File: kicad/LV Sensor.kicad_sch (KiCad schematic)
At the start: 22 parts, among them U1 MCP2518FD-xJHA, U2 LMR51603Y3DBVR, U3 XMSM0C1104SPW20R, U4 AP63205WU-7, U5 ATA6561-GAQW-N, U6 DSC1001DL5, U7 ADS114S06BIPBSR, U8 LM2662MX/NOPB

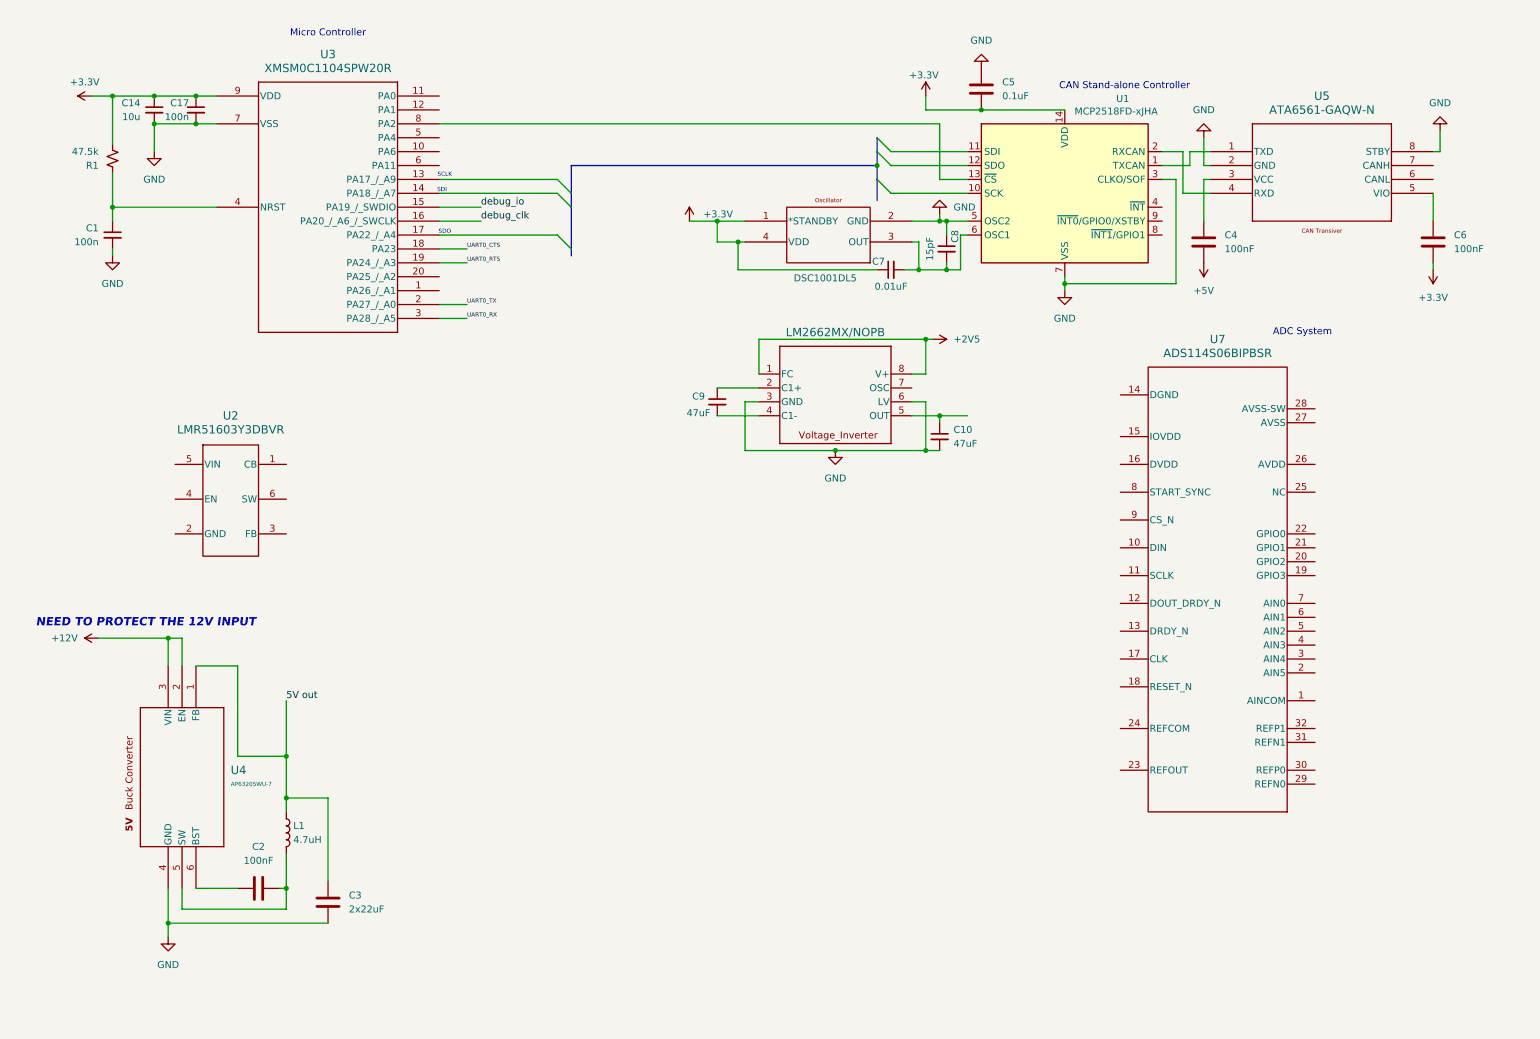
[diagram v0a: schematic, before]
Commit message: Pretty much finished everything for now. Just need to condition the analog inputs.
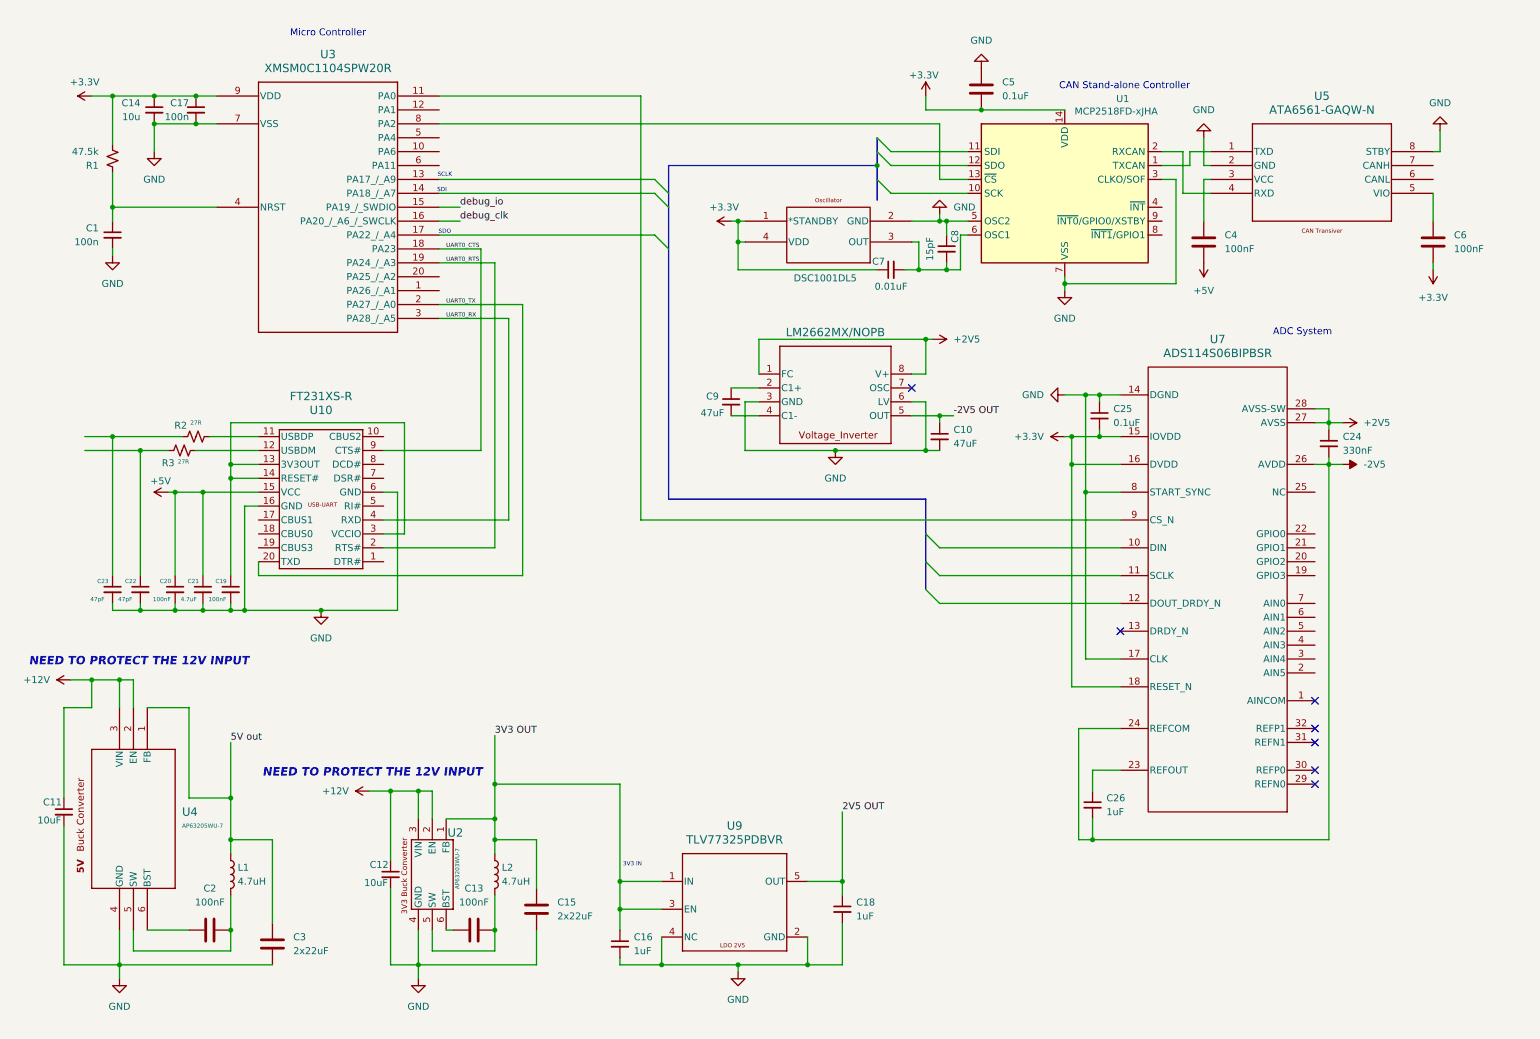
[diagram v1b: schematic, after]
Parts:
- removed U2: LMR51603Y3DBVR, DBV0006A-MFG-IPC_A, symbol LV-Sensor-Lib:LMR51603Y3DBVR
- added C11, C12: 10uF, symbol Device:C_Small
- added C13: 100nF, symbol Device:C
- added C15: 2x22uF, symbol Device:C
- added C16, C18, C26: 1uF, symbol Device:C_Small
- added C19, C20: 100nF, symbol Device:C_Small
- added C21: 4.7uF, symbol Device:C_Small
- added C22, C23: 47pF, symbol Device:C_Small
- added C24: 330nF, symbol Device:C_Small
- added C25: 0.1uF, symbol Device:C_Small
- added L2: 4.7uH, symbol Device:L
- added R2, R3: 27R, symbol Device:R_Small_US
- added U10: FT231XS-R, SSOP-20_FTD, symbol LV-Sensor-Lib:FT231XS-R
- added U2: AP63203WU-7, AP63203WU-7_DIO, symbol LV-Sensor-Lib:AP63203WU-7
- added U9: TLV77325PDBVR, DBV0005A-IPC_A, symbol LV-Sensor-Lib:TLV77325PDBVR
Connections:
- net +12V: now also C11.1, C12.1, U2.2 (EN), U2.3 (VIN)
- net +2V5: now also U7.27 (AVSS), U7.28 (AVSS-SW), C24.1
- net +3.3V: now also U7.15 (IOVDD), U7.16 (DVDD), U7.18 (RESET_N), C25.2
- net +5V: now also C20.1, C21.1, U10.15 (VCC)
- net GND: now also U7.14 (DGND), U7.17 (CLK), U7.8 (START_SYNC), C11.2, C12.2, C15.1, C16.2, C18.2, C19.2, C20.2, C21.2, C22.2, C23.2, C25.1, U10.16 (GND), U10.6 (GND), U2.4 (GND), U9.2 (GND), U9.4 (NC)
- net UART0_CTS: now also U10.9 (CTS#)
- net UART0_RTS: now also U10.2 (RTS#)
- net UART0_RX: now also U10.4 (RXD)
- net UART0_TX: now also U10.20 (TXD)
- net -2V5 OUT: now reaches C10.1, U8.5 (OUT)
- net at U7.23 (REFOUT): now also C26.1
- net -2V5: now reaches U7.24 (REFCOM)
- net -2V5: now also U7.26 (AVDD), C24.2, C26.2
- net at U7.9 (CS_N): now also U3.11 (PA0)
- new net: C23.1, R2.1
- new net: C22.1, R3.1
- new net: R3.2, U10.12 (USBDM)
- new net: R2.2, U10.11 (USBDP)
- new net: C19.1, U10.13 (3V3OUT), U10.14 (RESET#), U10.3 (VCCIO)
- new net: C13.1, U2.6 (BST)
- new net: C13.2, L2.2, U2.5 (SW)
- new net 2V5 OUT: C18.1, U9.5 (OUT)
- new net 3V3 OUT: C15.2, C16.1, L2.1, U2.1 (FB), U9.1 (IN), U9.3 (EN)
- no-connect marks 0 -> 7
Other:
- note added: "3V3 IN"
- moved on the sheet: C2, C3, C9, L1, U4

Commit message: 09-05-2025 Finished Revision.1 of LV Sensor Board
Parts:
- added C27: 22uF, Capacitor_SMD:C_1206_3216Metric_Pad1.33x1.80mm_HandSolder, symbol Device:C
- C1, C17: specs 100nF, 250VDC, X7R, 10%, -55C, +125C -> 100nF, 250VDC, X7R, +/-10%, -55C to +125C; unit x10 0.062 -> 0.042
- C10, C9: footprint (none) -> Capacitor_SMD:C_1206_3216Metric_Pad1.33x1.80mm_HandSolder; mouser (none) -> https://www.mouser.com/ProductDetail/Walsin/1206N470J500CT?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; specs (none) -> 47 pF, 60VDC, +/-5%, -55C to 125C; unit x10 (none) -> 0.058
- C11, C12: footprint (none) -> Capacitor_SMD:C_1206_3216Metric_Pad1.33x1.80mm_HandSolder; mouser (none) -> https://www.mouser.com/ProductDetail/Walsin/1206X106J250CT?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; specs (none) -> 10 uF, 25 VDC, +/-5%, -55C to +85; unit x10 (none) -> 0.202
- C13, C2: footprint (none) -> Capacitor_SMD:C_1206_3216Metric_Pad1.33x1.80mm_HandSolder; mouser (none) -> https://www.mouser.com/ProductDetail/Murata-Electronics/GRT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; specs (none) -> 0.1 uF, 1% tolerance, -55 to +125C; unit x10 (none) -> 0.583
- C14: unit x10 0.07 -> 00.07
- C15, C3: value 2x22uF -> 22uF; footprint (none) -> Capacitor_SMD:C_1206_3216Metric_Pad1.33x1.80mm_HandSolder; mouser (none) -> https://www.mouser.com/ProductDetail/Samsung-Electro-Mechan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; specs (none) -> 22 uF, 25VDC, +/-10%, -55C to +85C; unit x10 (none) -> 0.076
- C16, C18, C26: footprint (none) -> Capacitor_SMD:C_1206_3216Metric_Pad1.33x1.80mm_HandSolder; mouser (none) -> https://www.mouser.com/ProductDetail/Samsung-Electro-Mechan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; specs (none) -> 1uF, 50 VDC, +/-10%, -55C to +125C; unit x10 (none) -> 0.049
- C19, C20, C4, C6: footprint (none) -> Capacitor_SMD:C_1206_3216Metric_Pad1.33x1.80mm_HandSolder; mouser (none) -> https://www.mouser.com/ProductDetail/Walsin/0402B104K100CT?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; specs (none) -> 0.1 uF, 10VDC, +/-10%, -55C to +125C; unit x10 (none) -> 00.04
- C21: footprint (none) -> Capacitor_SMD:C_1206_3216Metric_Pad1.33x1.80mm_HandSolder; mouser (none) -> https://www.mouser.com/ProductDetail/Samsung-Electro-Mechan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; specs (none) -> 4.7 uF, 25 VDC,+/-10%, -55C to +125C; unit x10 (none) -> 0.067
- C22, C23: footprint (none) -> Capacitor_SMD:C_1206_3216Metric_Pad1.33x1.80mm_HandSolder; mouser (none) -> https://www.mouser.com/ProductDetail/Walsin/1206B474K100CT?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; specs (none) -> 0.47 uF, 10 VDC, +/-10%, -55C to +125; unit x10 (none) -> 0.076
- C24: footprint (none) -> Capacitor_SMD:C_1206_3216Metric_Pad1.33x1.80mm_HandSolder; mouser (none) -> https://www.mouser.com/ProductDetail/Murata-Electronics/GRM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; specs (none) -> 0.33 uF, 63VDC, +/-10%, -55C to +125C; unit x10 (none) -> 0.031
- C25, C5: footprint (none) -> Capacitor_SMD:C_1206_3216Metric_Pad1.33x1.80mm_HandSolder; mouser (none) -> https://www.mouser.com/ProductDetail/Walsin/1206B104K251CT?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; specs (none) -> 100nF, 250VDC, X7R, +/-10%, -55C to +125C; unit x10 (none) -> 0.042
- C7: footprint (none) -> Capacitor_SMD:C_1206_3216Metric_Pad1.33x1.80mm_HandSolder; mouser (none) -> https://www.mouser.com/ProductDetail/Walsin/1206N103F250CT?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; specs (none) -> 0.01uF, 25 VDC, +/-1%, -55C to 125C; unit x10 (none) -> 0.242
- C8: footprint (none) -> Capacitor_SMD:C_1206_3216Metric_Pad1.33x1.80mm_HandSolder; mouser (none) -> https://www.mouser.com/ProductDetail/Walsin/1206N150F500CT?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; specs (none) -> 15 pF, 50 VDC, +/-1%, -55C to +125C; unit x10 (none) -> 00.23
- L1, L2: footprint (none) -> Inductor_SMD:L_TDK_NLV25_2.5x2.0mm; mouser (none) -> https://www.mouser.com/ProductDetail/Wurth-Elektronik/74479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; specs (none) -> 4.7 uH, 128 mOhms, 25 MHz, -55 to +150 C; unit x10 (none) -> 0.311
- R1: unit x10 0.04 -> 00.04
- R2, R3: footprint (none) -> Resistor_SMD:R_1206_3216Metric_Pad1.30x1.75mm_HandSolder; mouser (none) -> https://www.mouser.com/ProductDetail/KOA-Speer/RK73B2BTTD39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; specs (none) -> 39Ohms, 200V,1/4 W, 5%, -55 to +155 C; unit x10 (none) -> 0.022
- U1: footprint LV Sensor:MCP2518FDT -> LV-Sensor-Footprints-Lib:MCP2518FDT; unit x10 19.6 -> 19.60
- U10: footprint SSOP-20_FTD -> LV-Sensor-Footprints-Lib:SSOP-20_FTD; mouser (none) -> https://www.mouser.com/ProductDetail/FTDI/FT231XS-R?qs=Gp1Y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; specs (none) -> 480 Mb/s, USB 2.0, 2.97V-5.5V, 125uA-8mA, -40C to + 85C; unit x10 (none) -> 23.40
- U2: footprint AP63203WU-7_DIO -> LV-Sensor-Footprints-Lib:AP6320xWU-7_DIO; mouser (none) -> https://www.mouser.com/ProductDetail/Diodes-Incorporated/AP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; specs (none) -> 3.8V-3.2V In, 3.3V Out, 2A Out, 3.8V-32V, 1.1MHz, -40C to +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; unit x10 (none) -> 05.06
- U3: footprint TSSOP20_PW_TEX -> LV-Sensor-Footprints-Lib:TSSOP20_PW_TEX; mouser (none) -> https://www.mouser.com/ProductDetail/Texas-Instruments/XMSM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; specs (none) -> 20PIN, 12-bit, 16KB flash, 24MHz CPU, 1.62V-3.6V, 32kHz LFO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; unit x10 (none) -> 05.06
- U4: footprint SOIC_05WU-7_DIO -> LV-Sensor-Footprints-Lib:AP6320xWU-7_DIO; mouser (none) -> https://www.mouser.com/ProductDetail/Diodes-Incorporated/AP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; specs (none) -> 3.8V-3.2V In, 5V Out, 2A Out, 3.8V-32V, 1.1MHz, -40C to +85C; unit x10 (none) -> 05.06
- U5: footprint SOIC8_4P9X3P9MC_MCH -> LV-Sensor-Footprints-Lib:SOIC8_4P9X3P9MC_MCH; mouser (none) -> https://www.mouser.com/ProductDetail/Microchip-Technology/A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; specs (none) -> 5Mb/s, 1 Driver /1 Receiver, 4.5V - 5.5V,50mA Operating Cur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; unit x10 (none) -> 04.80
- U6: footprint CDFN4_2P5X2_MCH -> LV-Sensor-Footprints-Lib:CDFN4_2P5X2_MCH; unit x10 (none) -> 14.00
- U7: footprint PBS0032A_N -> LV-Sensor-Footprints-Lib:PBS0032A_N; unit x10 6.08 -> 60.80
- U8: footprint M08A -> LV-Sensor-Footprints-Lib:M08A; mouser (none) -> https://www.mouser.com/ProductDetail/Texas-Instruments/LM26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; specs (none) -> 200mA, 1.3 mA Operating Current, -1.5 V to -5.5 V, 75kHz, 7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; unit x10 (none) -> 14.10
- U9: footprint DBV0005A-IPC_A -> LV-Sensor-Footprints-Lib:DBV0005A-IPC_A; mouser (none) -> https://www.mouser.com/ProductDetail/Texas-Instruments/TLV7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; specs (none) -> 300-mA, 2.5V Out, 1 Output, 1.4V-5.5V, 600mV Dropout, 80dB 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; unit x10 (none) -> 0.068
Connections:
- net +3.3V: now also C6.1, U5.5 (VIO); no longer C6.2
- net +5V: now also C4.1, U5.3 (VCC); no longer C4.2
- net 5V out: now also C27.2
- net GND: now also C4.2, C6.2, C27.1
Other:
- moved on the sheet: C6

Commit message: 09-05-2025 "Finished" LV-Sensor-Can Board
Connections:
- net +3.3V: no longer U6.1 (*STANDBY)
- no-connect marks 7 -> 8
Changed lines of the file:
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@@
 	)
 	(junction
-		(at 143.51 50.8)
-		(diameter 0)
-		(color 0 0 0 0)
-	)
-	(junction
 		(at 180.34 86.36)
 		(diameter 0)
@@
 	)
 	(no_connect
+		(at 144.78 50.8)
+	)
+	(no_connect
 		(at 248.92 153.67)
 	)
@@
 	(wire
 		(pts
-			(xy 143.51 50.8) (xy 143.51 54.61)
-		)
-		(stroke
-			(width 0)
-			(type default)
-		)
-	)
-	(wire
-		(pts
 			(xy 143.51 54.61) (xy 143.51 59.69)
 		)
@@
 	(wire
 		(pts
-			(xy 142.24 50.8) (xy 143.51 50.8)
+			(xy 138.43 54.61) (xy 143.51 54.61)
 		)
 		(stroke
@@
 	(wire
 		(pts
-			(xy 143.51 50.8) (xy 144.78 50.8)
-		)
-		(stroke
-			(width 0)
-			(type default)
-		)
-	)
-	(wire
-		(pts
 			(xy 208.28 163.83) (xy 251.46 163.83)
 		)
@@
 	(symbol
 		(lib_id "power:+3.3V")
-		(at 142.24 50.8 90)
+		(at 138.43 54.61 90)
 		(unit 1)
 		(exclude_from_sim no)
@@
 		(fields_autoplaced yes)
 		(property "Reference" "#PWR010"
-			(at 146.05 50.8 0)
+			(at 142.24 54.61 0)
 			(effects
 				(font
@@
 		)
 		(property "Value" "+3.3V"
-			(at 140.97 48.26 90)
+			(at 137.16 52.07 90)
 			(effects
 				(font
@@
 		)
 		(property "Footprint" ""
-			(at 142.24 50.8 0)
+			(at 138.43 54.61 0)
 			(effects
 				(font
@@
 		)
 		(property "Datasheet" ""
-			(at 142.24 50.8 0)
+			(at 138.43 54.61 0)
 			(effects
 				(font
@@
 		)
 		(property "Description" "Power symbol creates a global label with name \"+3.3V\""
-			(at 142.24 50.8 0)
+			(at 138.43 54.61 0)
 			(effects
 				(font

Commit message: 09-06-2025 Fixed Some Changes
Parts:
- removed U1: MCP2518FD-xJHA, LV-Sensor-Footprints-Lib:MCP2518FDT, symbol LV-Sensor-Lib:MCP2517FD-xJHA
- removed U6: DSC1001DL5, LV-Sensor-Footprints-Lib:CDFN4_2P5X2_MCH, symbol LV-Sensor-Lib:DSC1001DL5-020.0000T
- added U11: DSC1001DL5-020.0000T, LV-Sensor-Footprints-Lib:CDFN4_2P5X2_MCH, symbol LV-Sensor-Lib:DSC1001DL5-020.0000T
- added U6: MCP2518FD-xJHA, LV-Sensor-Footprints-Lib:MCP2518FDT, symbol LV-Sensor-Lib:MCP2517FD-xJHA
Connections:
- net +3.3V: now also U11.2 (GND), U6.14 (VDD)
- net GND: now also U11.4 (VDD), U6.3 (CLKO/SOF), U6.5 (OSC2), U6.7 (VSS)
- net TXCAN: now reaches U5.1 (TXD)
- net TXCAN: now also U6.1 (TXCAN)
- net RXCAN: now reaches U5.4 (RXD)
- net RXCAN: now also U6.2 (RXCAN)
- net CANL: now reaches U5.6 (CANL)
- net CANH: now reaches U5.7 (CANH)
- net at C7.2, C8.2: now also U11.3 (OUT), U6.6 (OSC1)
- net CS: now reaches U3.8 (PA2)
- net CS: now also U6.13 (~{CS})
- new net SCK: U6.10 (SCK)
- new net SDI: U6.11 (SDI)
- new net SDO: U6.12 (SDO)
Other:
- moved on the sheet: C4, C6, U5

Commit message: 09-06-2025 Again
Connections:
- net +3.3V: no longer C7.1, U11.2 (GND)
- net GND: now also U11.2 (GND); no longer U11.4 (VDD)
- net at C8.2, U6.6 (OSC1): now also C7.1; no longer C7.2, U11.3 (OUT)
- new net +3V3: C7.2, U11.3 (OUT), U11.4 (VDD)
- no-connect marks 8 -> 11
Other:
- moved on the sheet: C1, C14, C17, C4, C5, C6, C7, C8, R1, U3, U5, U6

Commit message: 09-26-2005
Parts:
- removed C5: 0.1uF, Capacitor_SMD:C_1206_3216Metric_Pad1.33x1.80mm_HandSolder, symbol Device:C
- removed C7: 0.01uF, Capacitor_SMD:C_1206_3216Metric_Pad1.33x1.80mm_HandSolder, symbol Device:C_Small
- added C23, C25: 100nF, Capacitor_SMD:C_1206_3216Metric_Pad1.33x1.80mm_HandSolder, symbol Device:C
- added TP1, TP2, TP3, TP4, TP5, TP6, TP7, TP8: TestPoint, symbol Connector:TestPoint
- C19: renamed from C8; now not fitted; now left out of the parts list
- renumbered C23 to C1, C2 to C10, C3 to C11, C27 to C12, C12 to C13, C13 to C14, C26 to C17, C25 to C18, C1 to C2, C18 to C20, C24 to C21, C9 to C22, C4 to C24, C6 to C26, C10 to C27, C11 to C3, C22 to C4, C14 to C5, C20 to C6, C21 to C7, C17 to C8, C19 to C9, R3 to R2, R2 to R3, U4 to U1, U8 to U10, U3 to U2, U10 to U3, U2 to U4, U9 to U5, U11 to U7, U7 to U8, U5 to U9
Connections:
- net CS is gone; now on an unnamed net: U2.8 (PA2), U6.13 (~{CS})
- net SCK is gone; now on an unnamed net: U6.10 (SCK)
- net SDI is gone; now on an unnamed net: U6.11 (SDI)
- net SDO is gone; now on an unnamed net: U6.12 (SDO)
- net +3.3V: now also C24.1
- net +3V3: now also C19.1; no longer U7.3 (OUT)
- net +5V: now also C23.1, C25.1; no longer C24.1
- net GND: now also C19.2, C23.2, C25.2; no longer C19.1, U6.3 (CLKO/SOF), U6.5 (OSC2), U9.8 (STBY)
- net at U8.10 (DIN): now also U2.14 (PA18_/_A7)
- net at U8.11 (SCLK): now also U2.13 (PA17_/_A9)
- net at U8.12 (DOUT_DRDY_N): now also U2.17 (PA22_/_A4)
- net at U8.9 (CS_N): no longer U2.11 (PA0)
- net at U6.6 (OSC1): now also U7.3 (OUT); no longer C19.2
- net PA1: now reaches U2.12 (PA1)
- net at U6.4 (~{INT}): now also TP6.1
- net at U6.8 (~{INT1}/GPIO1): now also TP4.1
- net at U6.9 (~{INT0}/GPIO0/XSTBY): now also TP3.1
- net CANH renamed CAN_H
- net CANL renamed CAN_L
- net RXCAN: no longer names the net of U6.2 (RXCAN), U9.4 (RXD)
- net TXCAN: no longer names the net of U6.1 (TXCAN), U9.1 (TXD)
- net debug_clk: no longer names the net of U2.16 (PA20_/_A6_/_SWCLK)
- net debug_clk: now also TP2.1
- net debug_io: no longer names the net of U2.15 (PA19_/_SWDIO)
- net debug_io: now also TP1.1
- new net: TP5.1, U6.3 (CLKO/SOF)
- new net: TP8.1, U9.8 (STBY)
- new net: TP7.1, U6.5 (OSC2)
- new net PA0: U2.11 (PA0)
- no-connect marks 11 -> 8
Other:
- note added: "debug_clk"
- note added: "debug_io"
- note added: "pg.4 : leave floating?"
- note added: "size unspecified"
- note removed: "ADC System"
- note removed: "CAN Stand-alone Controller"
- note removed: "Micro Controller"
- note removed: "SCLK"
- note removed: "SDI"
- note removed: "SDO"
- moved on the sheet: C1, C10, C11, C12, C13, C14, C15, C16, C17, C18, C2, C20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
